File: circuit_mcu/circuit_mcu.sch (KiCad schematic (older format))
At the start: 32 parts, among them J1 Conn_01x06, J2 Conn_01x04, J3 Conn_01x04, J4 Conn_01x04, J6 Conn_02x03_Odd_Even, SW2 SW_Push, U1 ATmega328P-PU, U2 4N25, U4 TSR_1-2450, U7 L80-R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

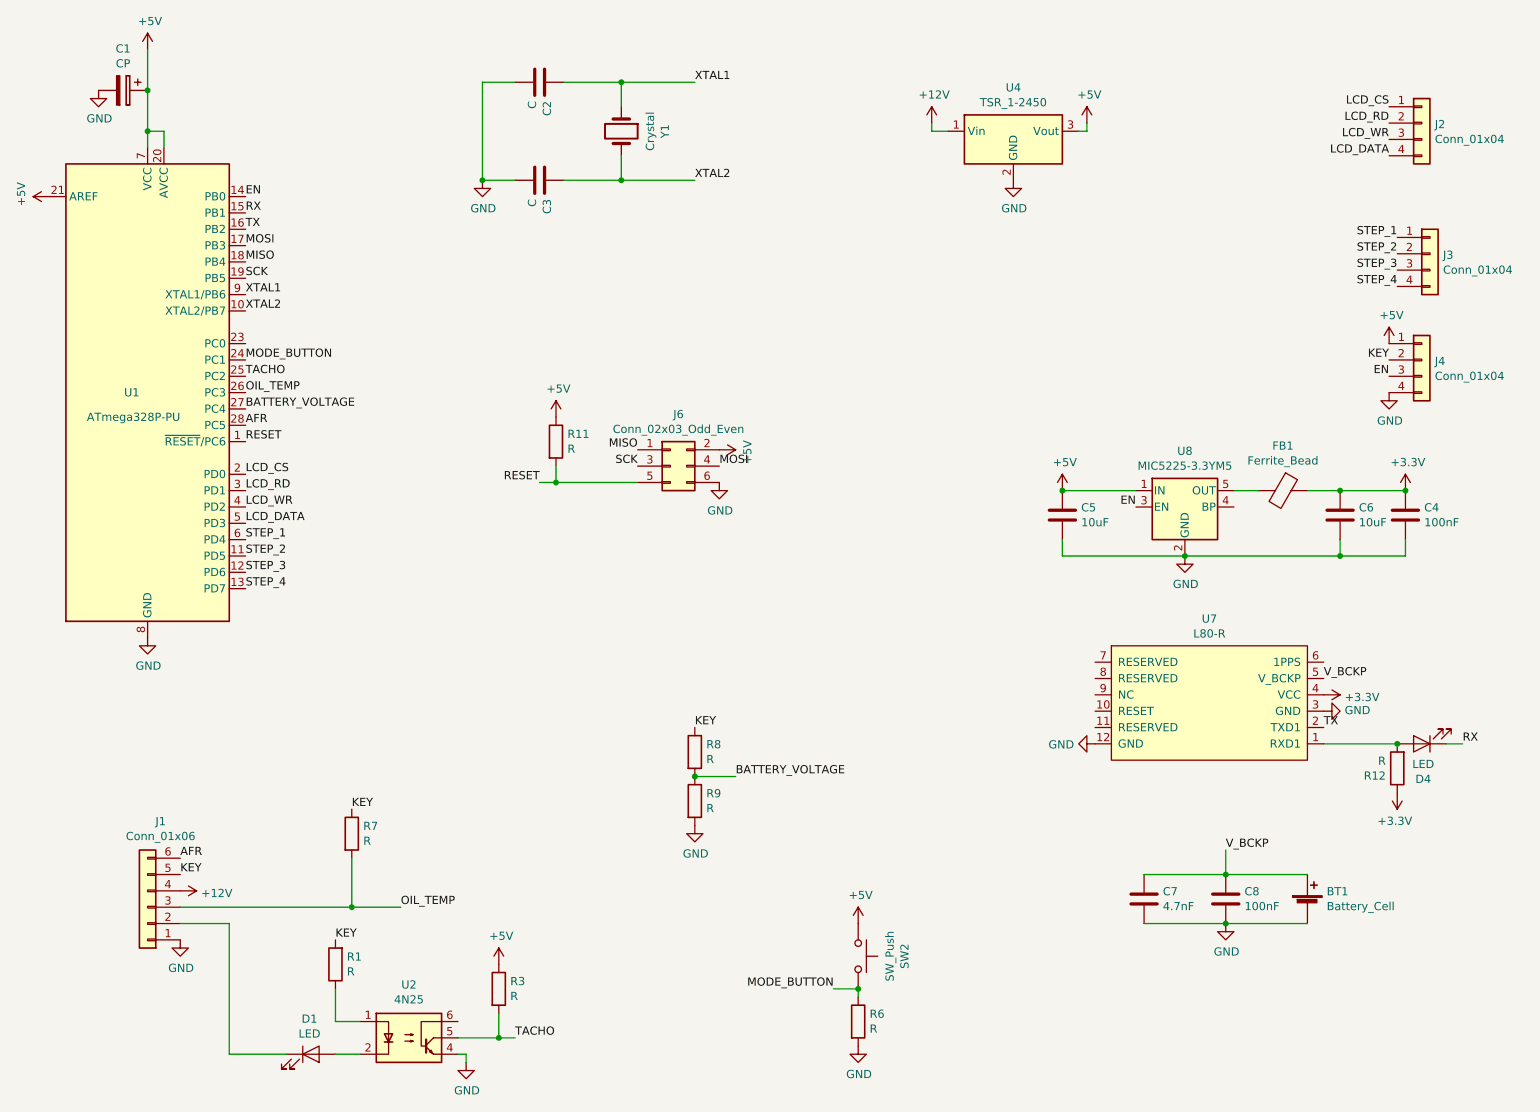
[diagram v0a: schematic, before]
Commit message: Removed unused LCD read net
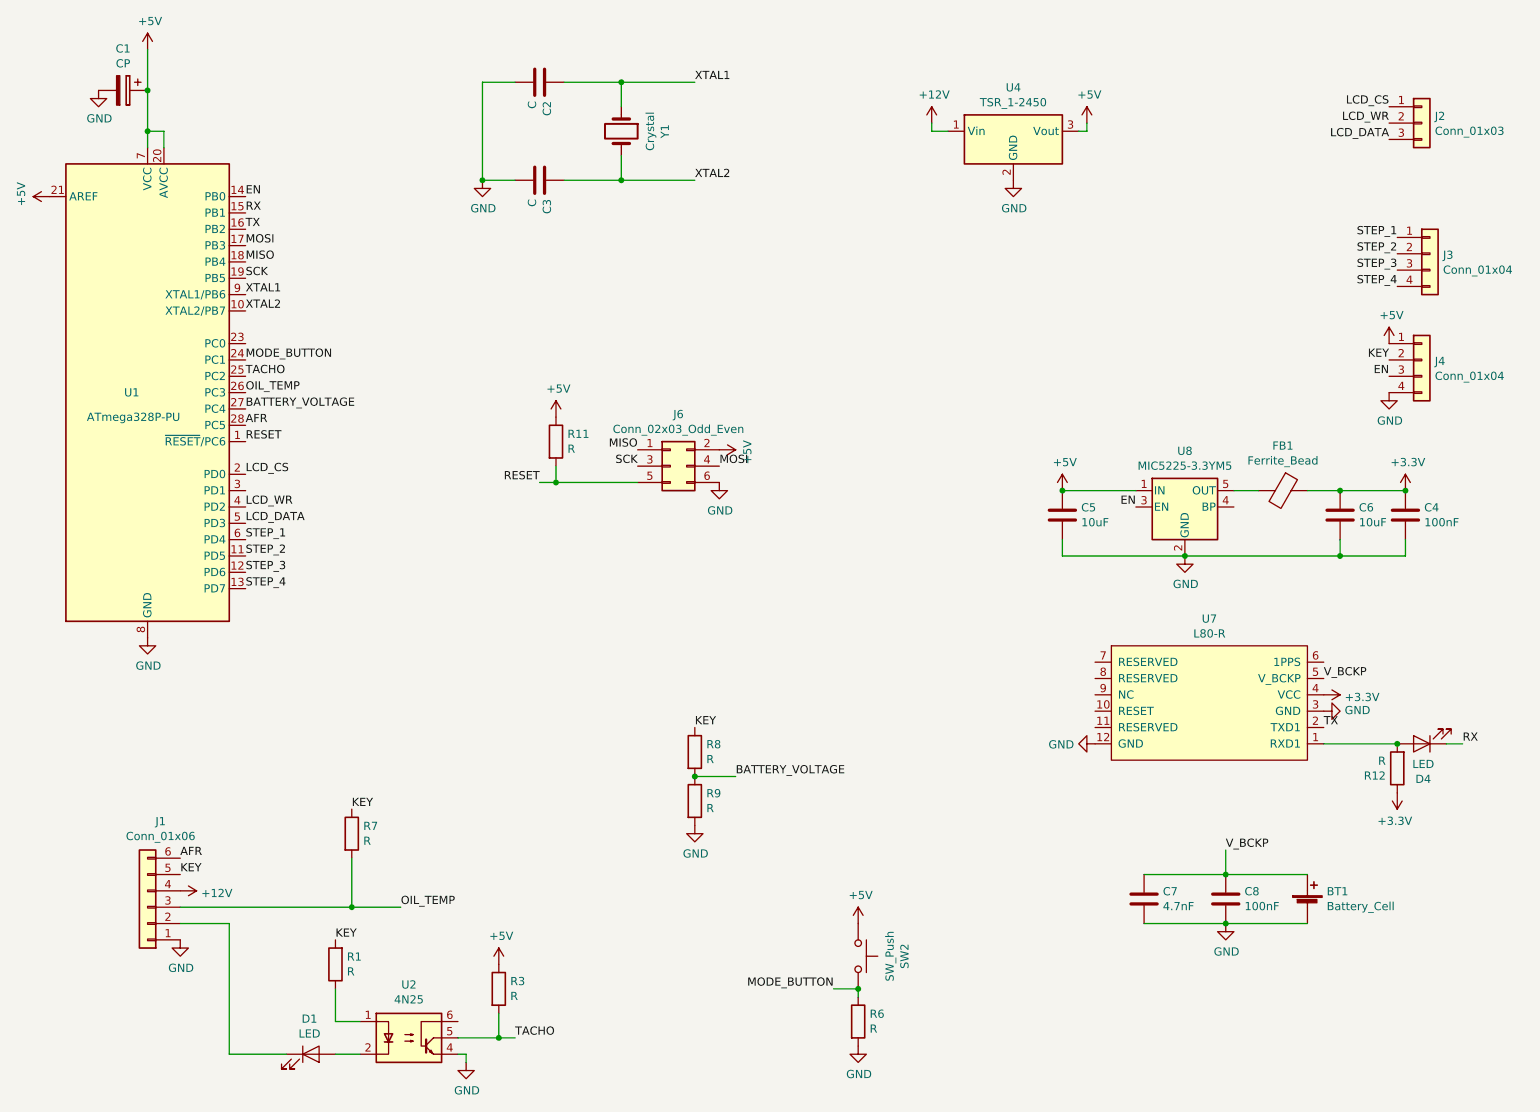
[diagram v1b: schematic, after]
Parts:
- removed J2: Conn_01x04, Connector_PinSocket_2.54mm:PinSocket_1x04_P2.54mm_Vertical, symbol Connector_Generic:Conn_01x04
- added J2: Conn_01x03, Connector_PinSocket_2.54mm:PinSocket_1x03_P2.54mm_Vertical, symbol Connector_Generic:Conn_01x03
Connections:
- net LCD_CS: now also J2.1 (Pin_1)
- net LCD_DATA: now also J2.3 (Pin_3)
- net LCD_WR: now also J2.2 (Pin_2)
- net LCD_RD: no longer names the net of U1.3 (PD1)
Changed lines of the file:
@@
 EESchema Schematic File Version 4
+LIBS:circuit_mcu-cache
 EELAYER 26 0
 EELAYER END
@@
 Text Label 2100 3400 0    50   ~ 0
 LCD_CS
-Text Label 2100 3500 0    50   ~ 0
-LCD_RD
 Text Label 2100 3600 0    50   ~ 0
 LCD_WR
@@
 Wire Wire Line
 	2000 6950 2350 6950
-$Comp
-L Connector_Generic:Conn_01x04 J2
-U 1 1 5D1D7F80
-P 9300 1250
-F 0 "J2" H 9380 1242 50  0000 L CNN
-F 1 "Conn_01x04" H 9380 1151 50  0000 L CNN
-F 2 "Connector_PinSocket_2.54mm:PinSocket_1x04_P2.54mm_Vertical" H 9300 1250 50  0001 C CNN
-F 3 "~" H 9300 1250 50  0001 C CNN
-	1    9300 1250
-	1    0    0    -1
-$EndComp
 Text Label 9150 1950 2    50   ~ 0
 STEP_1
@@
 LCD_CS
 Text Label 9100 1250 2    50   ~ 0
-LCD_RD
+LCD_WR
 Text Label 9100 1350 2    50   ~ 0
-LCD_WR
-Text Label 9100 1450 2    50   ~ 0
 LCD_DATA
 Text Label 2100 2000 0    50   ~ 0
@@
 Wire Wire Line
 	8100 5850 8100 5700
+$Comp
+L Connector_Generic:Conn_01x03 J2
+U 1 1 5D298ECD
+P 9300 1250
+F 0 "J2" H 9380 1292 50  0000 L CNN
+F 1 "Conn_01x03" H 9380 1201 50  0000 L CNN
+F 2 "Connector_PinSocket_2.54mm:PinSocket_1x03_P2.54mm_Vertical" H 9300 1250 50  0001 C CNN
+F 3 "~" H 9300 1250 50  0001 C CNN
+	1    9300 1250
+	1    0    0    -1
+$EndComp
 $EndSCHEMATC
